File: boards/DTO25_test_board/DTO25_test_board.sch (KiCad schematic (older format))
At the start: 8 parts

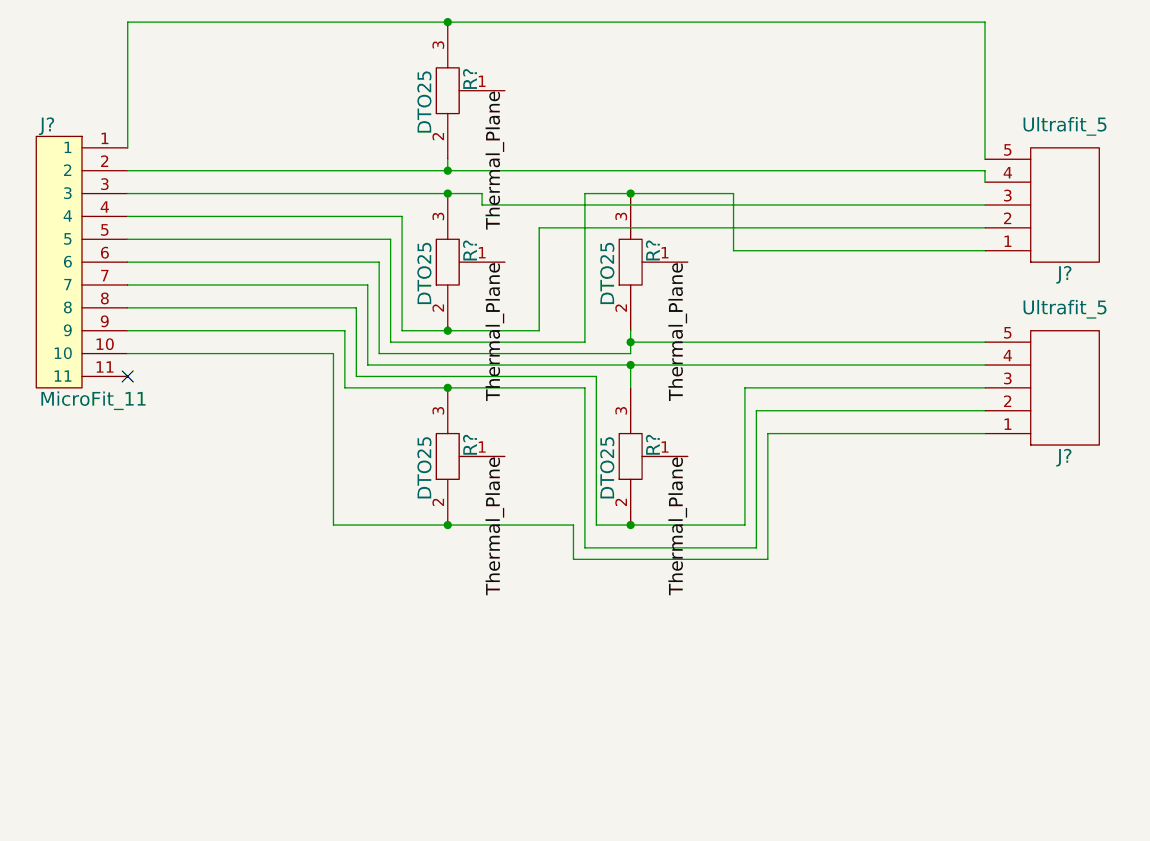
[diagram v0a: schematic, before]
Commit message: DTO25_test_board: Layout and tracing
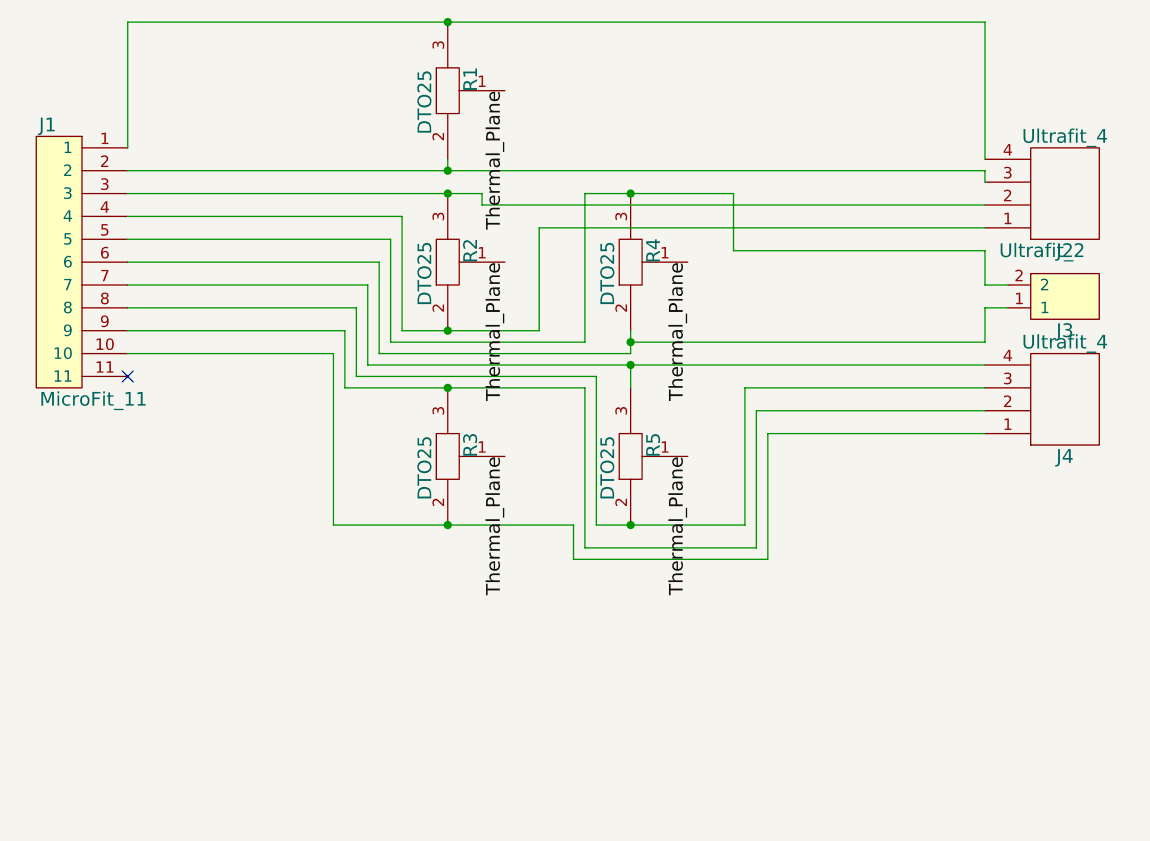
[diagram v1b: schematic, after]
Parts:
- removed J? (x2): Ultrafit_5, footprints:Ultrafit_4, symbol Ultrafit_5
- added J2, J4: Ultrafit_4, footprints:Ultrafit_4, symbol Ultrafit_4
- added J3: Ultrafit_2, footprints:Ultrafit_2, symbol Ultrafit_2
- gave numbers to parts that had none: 6
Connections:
- net at J1.4, R2.2: now also J2.1
- net at J1.3, R2.3: now also J2.2
- net at J1.2, R1.2: now also J2.3
- net at J1.1, R1.3: now also J2.4
- net at J1.10, R3.2: now also J4.1
- net at J1.9, R3.3: now also J4.2
- net at J1.8, R5.2: now also J4.3
- net at J1.7, R5.3: now also J4.4
- net at J1.6, R4.2: now also J3.1
- net at J1.5, R4.3: now also J3.2
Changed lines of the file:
@@
 $EndDescr
 $Comp
-L DTO25 R?
+L DTO25 R2
 U 1 1 5A01A039
 P 3300 2750
-F 0 "R?" H 3450 3050 60  0000 C CNN
+F 0 "R2" H 3450 3050 60  0000 C CNN
 F 1 "DTO25" H 3550 2850 60  0000 C CNN
 F 2 "footprints:DTO25" H 3300 2750 60  0001 C CNN
@@
 $EndComp
 $Comp
-L DTO25 R?
+L DTO25 R1
 U 1 1 5A01A083
 P 3300 2000
-F 0 "R?" H 3450 2300 60  0000 C CNN
+F 0 "R1" H 3450 2300 60  0000 C CNN
 F 1 "DTO25" H 3550 2100 60  0000 C CNN
 F 2 "footprints:DTO25" H 3300 2000 60  0001 C CNN
@@
 $EndComp
 $Comp
-L DTO25 R?
+L DTO25 R3
 U 1 1 5A01A0B5
 P 3300 3600
-F 0 "R?" H 3450 3900 60  0000 C CNN
+F 0 "R3" H 3450 3900 60  0000 C CNN
 F 1 "DTO25" H 3550 3700 60  0000 C CNN
 F 2 "footprints:DTO25" H 3300 3600 60  0001 C CNN
@@
 $EndComp
 $Comp
-L DTO25 R?
+L DTO25 R5
 U 1 1 5A01A0FE
 P 4100 3600
-F 0 "R?" H 4250 3900 60  0000 C CNN
+F 0 "R5" H 4250 3900 60  0000 C CNN
 F 1 "DTO25" H 4350 3700 60  0000 C CNN
 F 2 "footprints:DTO25" H 4100 3600 60  0001 C CNN
@@
 $EndComp
 $Comp
-L DTO25 R?
+L DTO25 R4
 U 1 1 5A01A130
 P 4100 2750
-F 0 "R?" H 4250 3050 60  0000 C CNN
+F 0 "R4" H 4250 3050 60  0000 C CNN
 F 1 "DTO25" H 4350 2850 60  0000 C CNN
 F 2 "footprints:DTO25" H 4100 2750 60  0001 C CNN
@@
 $EndComp
 $Comp
-L MicroFit_11 J?
+L MicroFit_11 J1
 U 1 1 5A01A1BD
 P 1700 2200
-F 0 "J?" H 1750 2050 60  0000 C CNN
+F 0 "J1" H 1750 2050 60  0000 C CNN
 F 1 "MicroFit_11" H 1950 850 60  0000 C CNN
 F 2 "footprints:Molex_MicroFit_3.0-11x3.00mm_Angled" H 1700 2200 60  0001 C CNN
@@
 	1    0    0    -1
 $EndComp
-$Comp
-L Ultrafit_5 J?
-U 1 1 5A01A35F
-P 6200 2700
-F 0 "J?" H 6200 3000 60  0000 C CNN
-F 1 "Ultrafit_5" H 6200 2350 60  0000 C CNN
-F 2 "footprints:Ultrafit_4" H 6100 2950 60  0001 C CNN
-F 3 "http://www.literature.molex.com/SQLImages/kelmscott/Molex/PDF_Images/987651-1008.pdf" H 6200 3050 60  0001 C CNN
-F 4 "Digi-Key" H 6200 2700 60  0001 C CNN "MFN"
-F 5 "Value" H 6200 2700 60  0001 C CNN "Package"
-F 6 "WM11667-ND" H 6200 2700 60  0001 C CNN "MPN"
-F 7 "https://www.digikey.com/product-detail/en/molex-llc/1722861105/WM11667-ND/5360132" H 6700 3550 60  0001 C CNN "PurchasingLink"
-	1    6200 2700
+Wire Wire Line
+	2100 2450 2100 1900
+Wire Wire Line
+	2100 1900 5850 1900
+Wire Wire Line
+	2100 2550 5850 2550
+Wire Wire Line
+	3500 2550 3500 2500
+Wire Wire Line
+	2100 2650 3650 2650
+Wire Wire Line
+	2100 2750 3300 2750
+Wire Wire Line
+	3300 2750 3300 3250
+Wire Wire Line
+	3300 3250 3900 3250
+Wire Wire Line
+	2100 2850 3250 2850
+Wire Wire Line
+	3250 2850 3250 3300
+Wire Wire Line
+	3250 3300 4100 3300
+Wire Wire Line
+	4100 3300 4100 2650
+Wire Wire Line
+	4100 2650 4750 2650
+Wire Wire Line
+	2100 2950 3200 2950
+Wire Wire Line
+	3200 2950 3200 3350
+Wire Wire Line
+	3200 3350 4300 3350
+Wire Wire Line
+	4300 3350 4300 3250
+Wire Wire Line
+	2100 3050 3150 3050
+Wire Wire Line
+	3150 3050 3150 3400
+Wire Wire Line
+	3150 3400 5850 3400
+Wire Wire Line
+	4300 3400 4300 3500
+Wire Wire Line
+	2100 3150 3100 3150
+Wire Wire Line
+	3100 3150 3100 3450
+Wire Wire Line
+	3100 3450 4150 3450
+Wire Wire Line
+	4150 3450 4150 4100
+Wire Wire Line
+	4150 4100 4800 4100
+Wire Wire Line
+	2100 3250 3050 3250
+Wire Wire Line
+	3050 3250 3050 3500
+Wire Wire Line
+	3050 3500 4100 3500
+Wire Wire Line
+	2100 3350 3000 3350
+Wire Wire Line
+	3000 3350 3000 4100
+Wire Wire Line
+	3000 4100 4050 4100
+Wire Wire Line
+	5850 1900 5850 2500
+Connection ~ 3500 1900
+Wire Wire Line
+	5850 2550 5850 2600
+Connection ~ 3500 2550
+Wire Wire Line
+	5850 2700 3650 2700
+Wire Wire Line
+	3650 2700 3650 2650
+Connection ~ 3500 2650
+Wire Wire Line
+	5850 2800 3900 2800
+Wire Wire Line
+	3900 2800 3900 3250
+Connection ~ 3500 3250
+Wire Wire Line
+	5850 2900 4750 2900
+Wire Wire Line
+	4750 2900 4750 2650
+Connection ~ 4300 2650
+Wire Wire Line
+	5850 3300 4300 3300
+Connection ~ 4300 3300
+Connection ~ 4300 3400
+Wire Wire Line
+	5850 3500 4800 3500
+Wire Wire Line
+	4800 3500 4800 4100
+Connection ~ 4300 4100
+Wire Wire Line
+	5850 3600 4850 3600
+Wire Wire Line
+	4850 3600 4850 4200
+Wire Wire Line
+	4850 4200 4100 4200
+Wire Wire Line
+	4100 4200 4100 3500
+Connection ~ 3500 3500
+Wire Wire Line
+	4050 4100 4050 4250
+Wire Wire Line
+	4050 4250 4900 4250
+Wire Wire Line
+	4900 4250 4900 3700
+Wire Wire Line
+	4900 3700 5850 3700
+Connection ~ 3500 4100
+Text Label 3750 2200 3    60   ~ 0
+Thermal_Plane
+Text Label 3750 2950 3    60   ~ 0
+Thermal_Plane
+Text Label 4550 2950 3    60   ~ 0
+Thermal_Plane
+Text Label 3750 3800 3    60   ~ 0
+Thermal_Plane
+Text Label 4550 3800 3    60   ~ 0
+Thermal_Plane
+NoConn ~ 2100 3450
+$Comp
+L Ultrafit_4 J2
+U 1 1 5A02FDEF
+P 6200 2600
+F 0 "J2" H 6200 2900 60  0000 C CNN
+F 1 "Ultrafit_4" H 6200 2400 60  0000 C CNN
+F 2 "footprints:Ultrafit_4" H 6100 2850 60  0001 C CNN
+F 3 "http://www.literature.molex.com/SQLImages/kelmscott/Molex/PDF_Images/987651-1008.pdf" H 6200 2950 60  0001 C CNN
+F 4 "Digi-Key" H 6200 2600 60  0001 C CNN "MFN"
+F 5 "Value" H 6200 2600 60  0001 C CNN "Package"
+F 6 "WM11574-ND" H 6200 2600 60  0001 C CNN "MPN"
+F 7 "WM11564-ND" H 6600 3350 60  0001 C CNN "MPN2"
+F 8 "https://www.digikey.com/products/en?keywords=WM11574-ND" H 6700 3450 60  0001 C CNN "PurchasingLink"
+F 9 "https://www.digikey.com/product-detail/en/molex-llc/1722561004/WM11564-ND/5291228" H 6800 3550 60  0001 C CNN "PurchasingLink2"
+	1    6200 2600
 	-1   0    0    1
 $EndComp
 $Comp
-L Ultrafit_5 J?
-U 1 1 5A01A3BF
+L Ultrafit_4 J4
+U 1 1 5A02FE73
 P 6200 3500
-F 0 "J?" H 6200 3800 60  0000 C CNN
-F 1 "Ultrafit_5" H 6200 3150 60  0000 C CNN
+F 0 "J4" H 6200 3800 60  0000 C CNN
+F 1 "Ultrafit_4" H 6200 3300 60  0000 C CNN
 F 2 "footprints:Ultrafit_4" H 6100 3750 60  0001 C CNN
 F 3 "http://www.literature.molex.com/SQLImages/kelmscott/Molex/PDF_Images/987651-1008.pdf" H 6200 3850 60  0001 C CNN
 F 4 "Digi-Key" H 6200 3500 60  0001 C CNN "MFN"
 F 5 "Value" H 6200 3500 60  0001 C CNN "Package"
-F 6 "WM11667-ND" H 6200 3500 60  0001 C CNN "MPN"
-F 7 "https://www.digikey.com/product-detail/en/molex-llc/1722861105/WM11667-ND/5360132" H 6700 4350 60  0001 C CNN "PurchasingLink"
+F 6 "WM11574-ND" H 6200 3500 60  0001 C CNN "MPN"
+F 7 "WM11564-ND" H 6600 4250 60  0001 C CNN "MPN2"
+F 8 "https://www.digikey.com/products/en?keywords=WM11574-ND" H 6700 4350 60  0001 C CNN "PurchasingLink"
+F 9 "https://www.digikey.com/product-detail/en/molex-llc/1722561004/WM11564-ND/5291228" H 6800 4450 60  0001 C CNN "PurchasingLink2"
 	1    6200 3500
 	-1   0    0    1
 $EndComp
-Wire Wire Line
-	2100 2450 2100 1900
-Wire Wire Line
-	2100 1900 5850 1900
-Wire Wire Line
-	2100 2550 5850 2550
-Wire Wire Line
-	3500 2550 3500 2500
-Wire Wire Line
-	2100 2650 3650 2650
-Wire Wire Line
-	2100 2750 3300 2750
-Wire Wire Line
-	3300 2750 3300 3250
-Wire Wire Line
-	3300 3250 3900 3250
-Wire Wire Line
-	2100 2850 3250 2850
-Wire Wire Line
-	3250 2850 3250 3300
-Wire Wire Line
-	3250 3300 4100 3300
-Wire Wire Line
-	4100 3300 4100 2650
-Wire Wire Line
-	4100 2650 4750 2650
-Wire Wire Line
-	2100 2950 3200 2950
-Wire Wire Line
-	3200 2950 3200 3350
-Wire Wire Line
-	3200 3350 4300 3350
-Wire Wire Line
-	4300 3350 4300 3250
-Wire Wire Line
-	2100 3050 3150 3050
-Wire Wire Line
-	3150 3050 3150 3400
-Wire Wire Line
-	3150 3400 5850 3400
-Wire Wire Line
-	4300 3400 4300 3500
-Wire Wire Line
-	2100 3150 3100 3150
-Wire Wire Line
-	3100 3150 3100 3450
-Wire Wire Line
-	3100 3450 4150 3450
-Wire Wire Line
-	4150 3450 4150 4100
-Wire Wire Line
-	4150 4100 4800 4100
-Wire Wire Line
-	2100 3250 3050 3250
-Wire Wire Line
-	3050 3250 3050 3500
-Wire Wire Line
-	3050 3500 4100 3500
-Wire Wire Line
-	2100 3350 3000 3350
-Wire Wire Line
-	3000 3350 3000 4100
-Wire Wire Line
-	3000 4100 4050 4100
-Wire Wire Line
-	5850 1900 5850 2500
-Connection ~ 3500 1900
-Wire Wire Line
-	5850 2550 5850 2600
-Connection ~ 3500 2550
-Wire Wire Line
-	5850 2700 3650 2700
-Wire Wire Line
-	3650 2700 3650 2650
-Connection ~ 3500 2650
-Wire Wire Line
-	5850 2800 3900 2800
-Wire Wire Line
-	3900 2800 3900 3250
-Connection ~ 3500 3250
-Wire Wire Line
-	5850 2900 4750 2900
-Wire Wire Line
-	4750 2900 4750 2650
-Connection ~ 4300 2650
-Wire Wire Line
-	5850 3300 4300 3300
-Connection ~ 4300 3300
-Connection ~ 4300 3400
-Wire Wire Line
-	5850 3500 4800 3500
-Wire Wire Line
-	4800 3500 4800 4100
-Connection ~ 4300 4100
-Wire Wire Line
-	5850 3600 4850 3600
-Wire Wire Line
-	4850 3600 4850 4200
-Wire Wire Line
-	4850 4200 4100 4200
-Wire Wire Line
-	4100 4200 4100 3500
-Connection ~ 3500 3500
-Wire Wire Line
-	4050 4100 4050 4250
-Wire Wire Line
-	4050 4250 4900 4250
-Wire Wire Line
-	4900 4250 4900 3700
-Wire Wire Line
-	4900 3700 5850 3700
-Connection ~ 3500 4100
-Text Label 3750 2200 3    60   ~ 0
-Thermal_Plane
-Text Label 3750 2950 3    60   ~ 0
-Thermal_Plane
-Text Label 4550 2950 3    60   ~ 0
-Thermal_Plane
-Text Label 3750 3800 3    60   ~ 0
-Thermal_Plane
-Text Label 4550 3800 3    60   ~ 0
-Thermal_Plane
-NoConn ~ 2100 3450
+$Comp
+L Ultrafit_2 J3
+U 1 1 5A02FF03
+P 6200 3100
+F 0 "J3" H 6200 3250 60  0000 C CNN
+F 1 "Ultrafit_2" H 6300 2900 60  0000 C CNN
+F 2 "footprints:Ultrafit_2" H 6100 3150 60  0001 C CNN
+F 3 "" H 6200 3250 60  0001 C CNN
+F 4 "https://www.digikey.com/product-detail/en/molex-llc/1722861102/WM11570-ND/5344267" H 6300 3350 60  0001 C CNN "PurchasingLink"
+F 5 "Digi-Key" H 6400 3450 60  0001 C CNN "MFN"
+F 6 "WM11570-ND" H 6500 3550 60  0001 C CNN "MPN"
+F 7 "Value" H 6600 3650 60  0001 C CNN "Package"
+	1    6200 3100
+	-1   0    0    1
+$EndComp
+Wire Wire Line
+	5950 3050 5850 3050
+Wire Wire Line
+	5850 3050 5850 2900
+Wire Wire Line
+	5950 3150 5850 3150
+Wire Wire Line
+	5850 3150 5850 3300
 $EndSCHEMATC

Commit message: DTO@% test board MKII
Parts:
- removed J1: MicroFit_11, footprints:Molex_MicroFit_3.0-11x3.00mm_Angled, symbol MicroFit_11
- removed J2, J4: Ultrafit_4, footprints:Ultrafit_4, symbol Ultrafit_4
- removed J3: Ultrafit_2, footprints:Ultrafit_2, symbol Ultrafit_2
- added P1, P2: CONN_02X03, footprints:Pin_Header_Straight_2x03, symbol CONN_02X03
- added R6: DTO25, footprints:DTO25, symbol DTO25
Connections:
- net at R2.2: now also P1.4 (P4)
- net at R2.3: now also P1.3 (P3)
- net at R1.2: now also P1.5 (P5)
- net at R1.3: now also P1.6 (P6)
- net at R3.2: now also P1.2 (P2)
- net at R3.3: now also P1.1 (P1)
- net at R5.2: now also P2.3 (P3)
- net at R5.3: now also P2.4 (P4)
- net at R4.2: now also P2.1 (P1)
- net at R4.3: now also P2.2 (P2)
- removed net Thermal_Plane: R1.1, R2.1, R3.1, R4.1, R5.1
- new net: P2.6 (P6), R6.2
- new net: P2.5 (P5), R6.3
- new net ThermalPlane1: R1.1
- new net ThermalPlane2: R2.1
- new net ThermalPlane3: R3.1
- new net ThermalPlane4: R4.1
- new net ThermalPlane5: R5.1
- new net ThermalPlane6: R6.1
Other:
- moved on the sheet: R1, R2, R3
